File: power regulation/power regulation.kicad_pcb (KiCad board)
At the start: 4 copper layers, 175 x 100 mm, 90 parts, among them J1 Conn_01x02_Pin, J2 Conn_01x02_Pin, J3 Conn_01x02_Pin, M1 TO-236AB_SOT23_NEX, M2 TO-236AB_SOT23_NEX, U1 LT8640SEV_PBF, U2 LT8640SEV_PBF, U3 LT8619EDD-TRPBF

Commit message: start work on clearance fixes.
modified 8V regulator footprint, added not MAX rtd module not connected.
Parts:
- added REF**: QFN65P500X500X80-21N_MAXRTD_Pinless, Library:QFN65P500X500X80-21N_MAXRTD_Pinless, F.Cu at (239.2, 88.1)

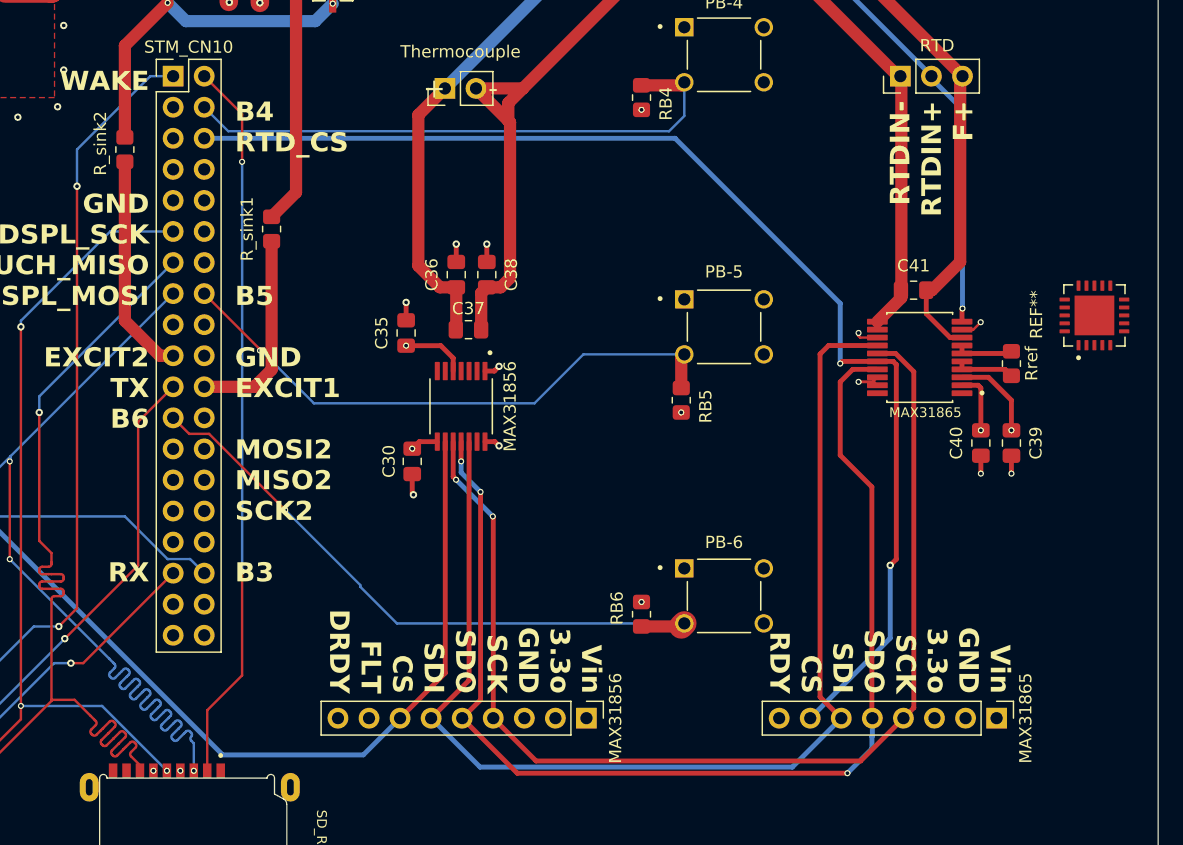
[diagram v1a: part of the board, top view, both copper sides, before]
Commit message: Fully integrate new Max RTD module.
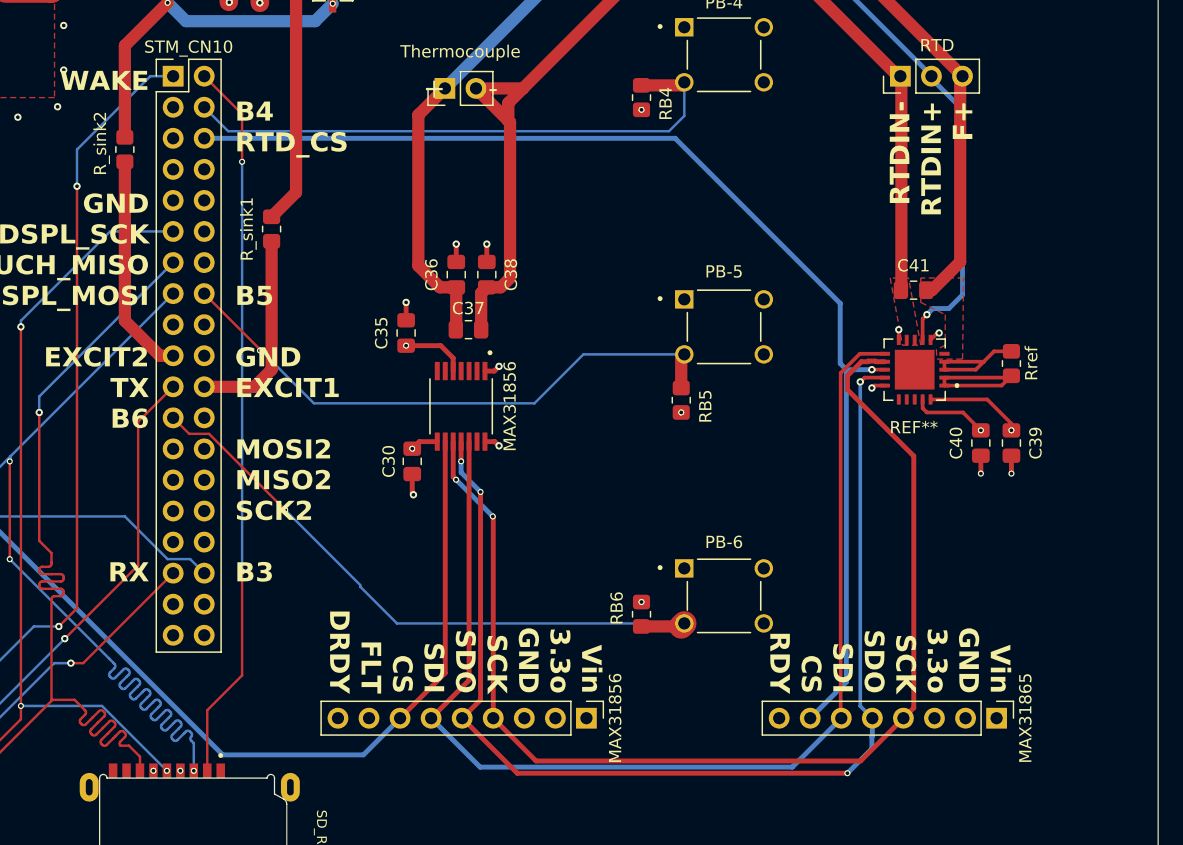
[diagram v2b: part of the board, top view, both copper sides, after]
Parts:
- removed the MAX31865 at (224.9, 91.5)
- moved REF** 15.4 mm to (224.5, 92.5), turned to 180 degrees
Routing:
- net BIAS: track 4.91 -> 12.0 mm
- net RTD+: track 44.6 -> 38.9 mm
- net ISENSOR: track 4.76 -> 9.96 mm
- net GND: track 120.7 -> 116.6 mm
- net RTD-: track 39.9 -> 35.9 mm
- net RTDSens: track 38.1 -> 41.7 mm
- net RTD_CS: track 99.1 -> 96.1 mm, vias 2 -> 1
- net MAX_SDI: track 96.2 -> 93.3 mm
- net MAX_SDO: track 94.7 -> 92.7 mm, vias 3 -> 4
- net MAX_SCK: track 92.7 -> 94.6 mm
- net /3.3V: track 92.9 -> 94.7 mm
- added copper zone on F.Cu, net RTD+
- added copper zone on F.Cu, net RTD-

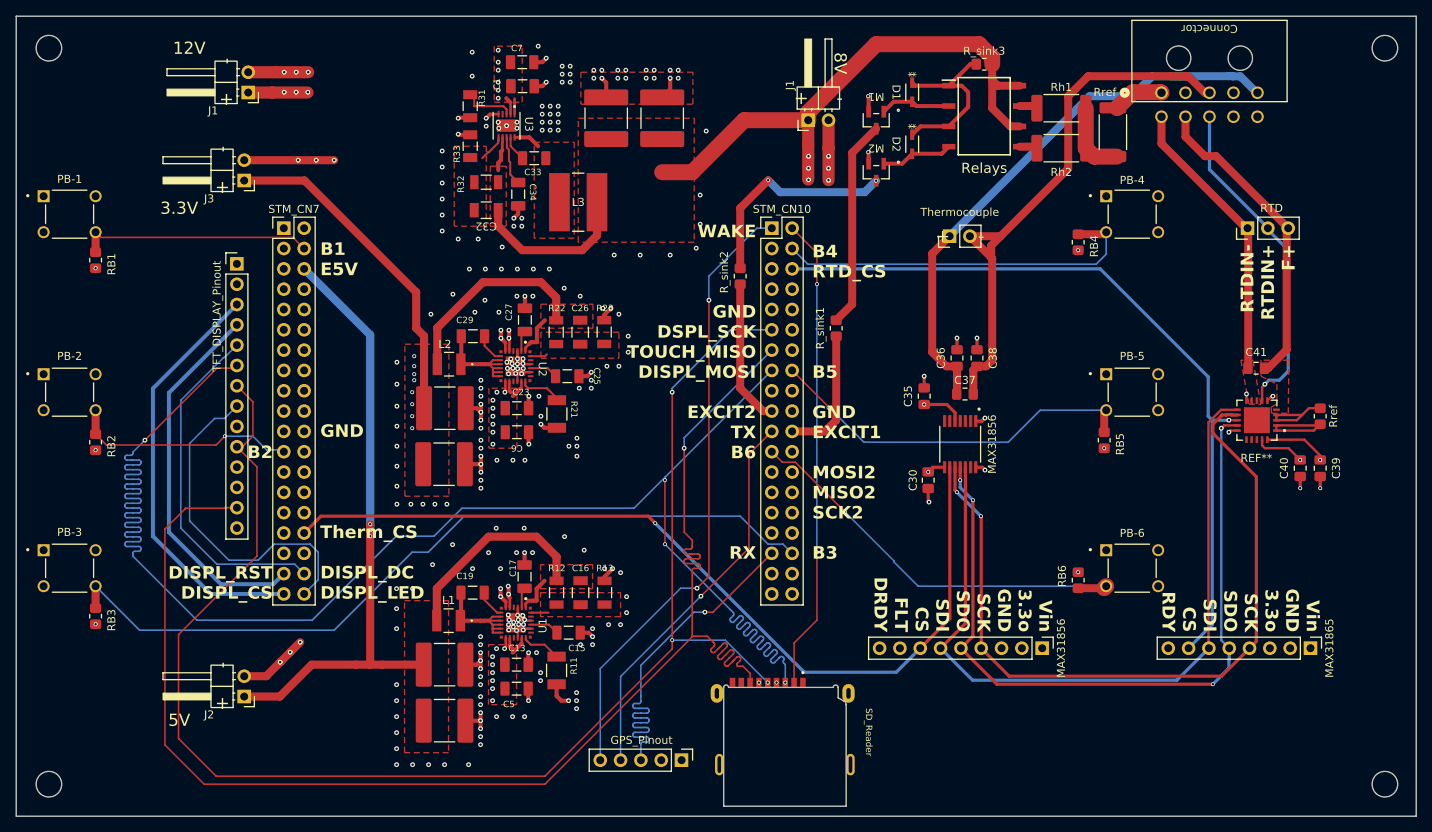
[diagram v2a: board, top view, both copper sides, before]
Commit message: Add holes for screen.
Moved traces and a couple comonents to accomodate.
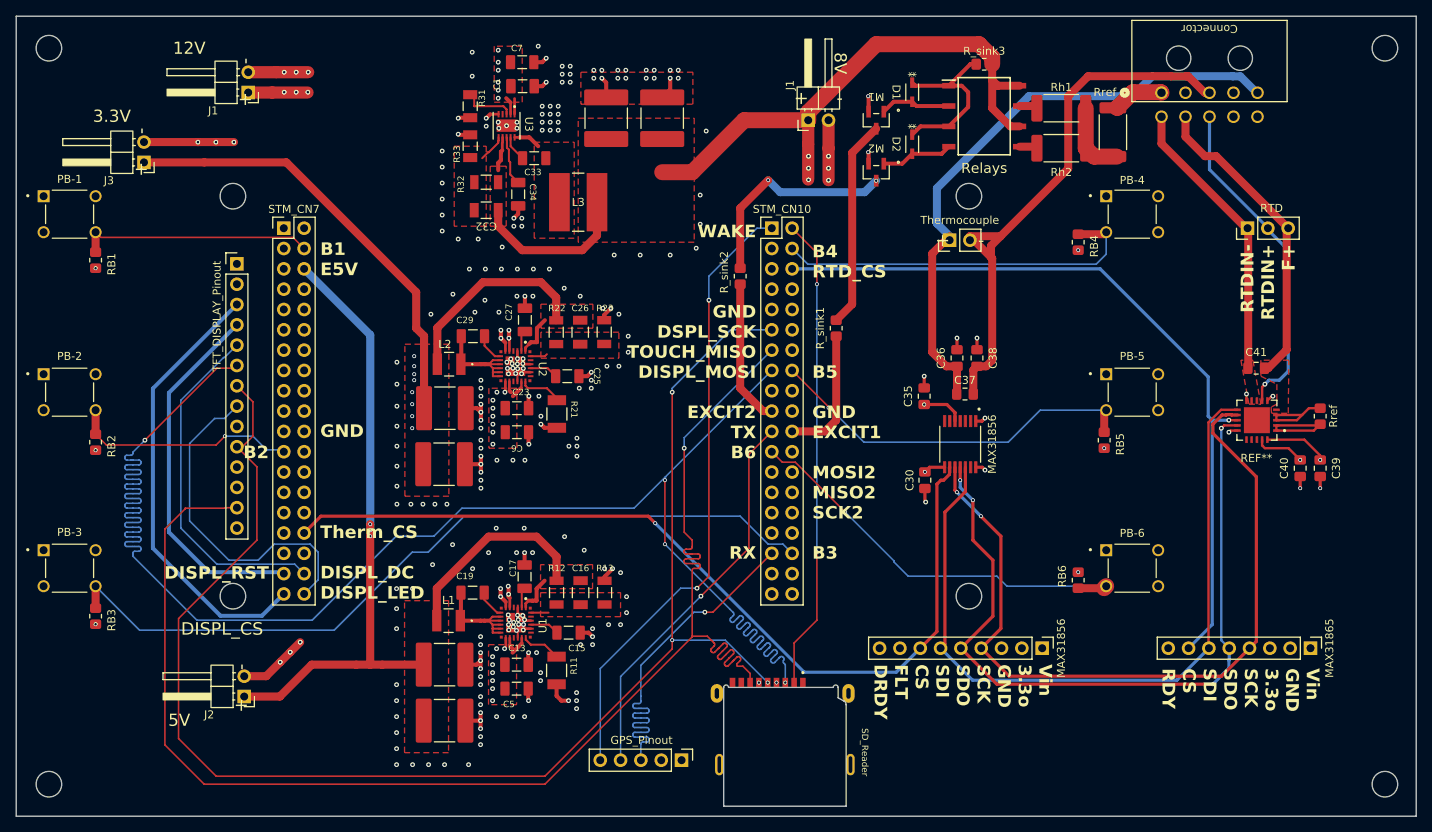
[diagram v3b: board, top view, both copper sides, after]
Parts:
- added hole: MountingHole_3.2mm_M3, MountingHole:MountingHole_3.2mm_M3, F.Cu at (96.5, 64.5)
- added hole: MountingHole_3.2mm_M3, MountingHole:MountingHole_3.2mm_M3, F.Cu at (188.5, 114.5)
- added hole: MountingHole_3.2mm_M3, MountingHole:MountingHole_3.2mm_M3, F.Cu at (188.5, 64.5)
- added hole: MountingHole_3.2mm_M3, MountingHole:MountingHole_3.2mm_M3, F.Cu at (96.5, 114.5)
- moved J3 12.7 mm to (85.4, 60.3)
- moved Thermocouple 0.50 mm to (186.1, 70.0)
- moved C30 0.41 mm to (183.0, 100.0)
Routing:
- net /3.3V: track 94.7 -> 108.6 mm
- net Thermocouple+: track 70.4 -> 76.1 mm
- net DISPL_CS: track 52.7 -> 55.8 mm
- net MAX_SDO: track 92.7 -> 94.8 mm
- net MAX_SCK: track 94.6 -> 96.6 mm
- net DISPL_RST: track 47.0 -> 45.9 mm
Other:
- board text added: "B2 DISPL_RST"
- board text added: "DISPL_CS"
- board text removed: "B2 DISPL_RST DISPL_CS"

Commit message: Connect Max modules to STM header.
Also added so extra silkscreening.
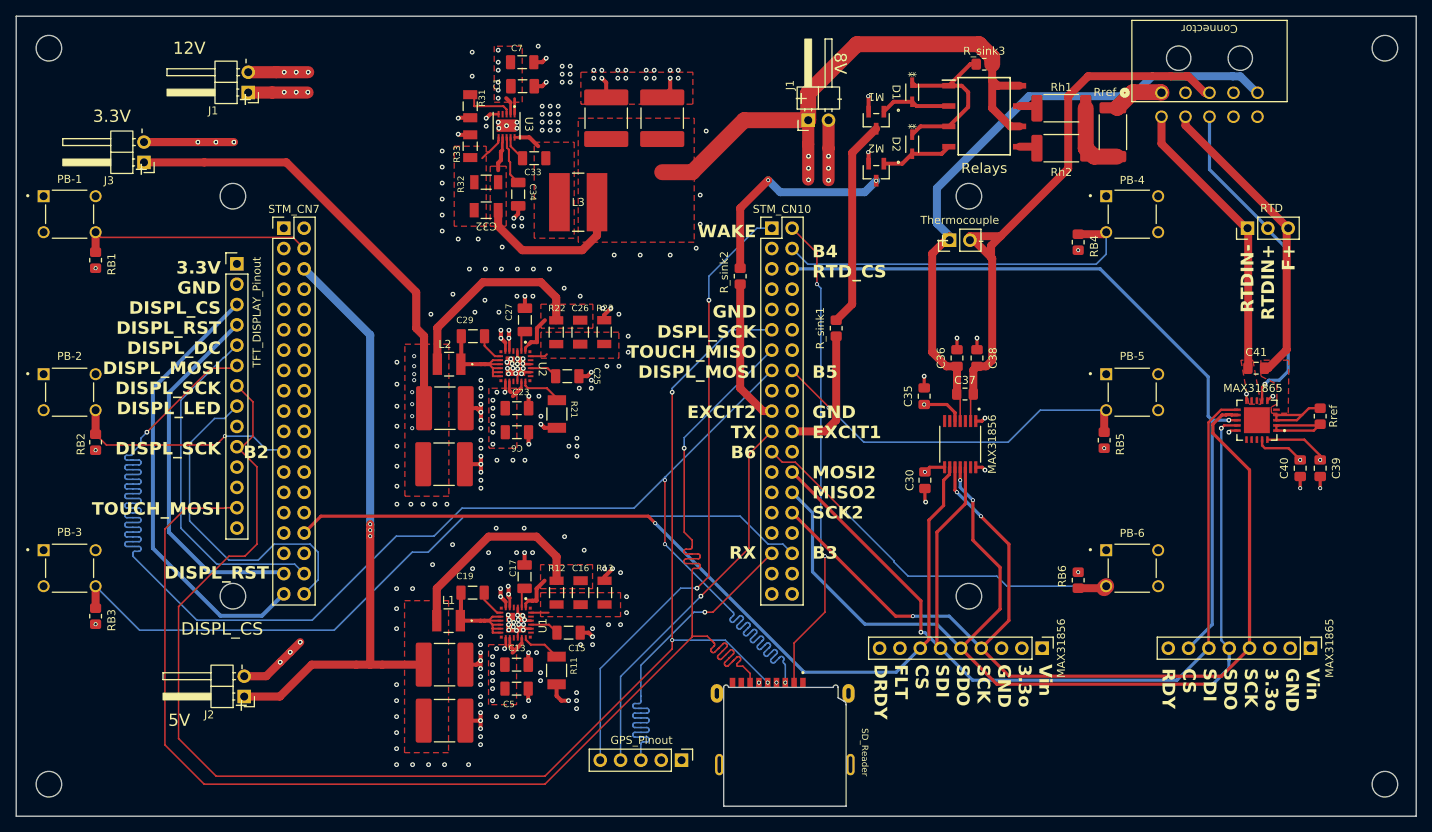
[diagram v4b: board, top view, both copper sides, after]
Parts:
- renumbered REF** to MAX31865
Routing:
- net MAX_SDO: track 94.8 -> 129.0 mm
- net MAX_SCK: track 96.6 -> 127.4 mm, vias 2 -> 3
- net MAX_SDI: track 93.3 -> 123.6 mm, vias 0 -> 1
- net Thermocouple+: track 76.1 -> 79.7 mm
- net Thermocouple-: track 70.3 -> 73.8 mm
- net /8V: track 97.3 -> 98.7 mm
- net DISPL_SCK: track 183.7 -> 184.9 mm
- net SD_CS: track 59.3 -> 60.1 mm
- net RTD+: track 38.9 -> 38.1 mm
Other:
- board text added: "3.3V GND DISPL_CS DISPL_RST DISPL_DC DISPL_MOSI DISPL_SCK DISPL_LED DISPL_SCK TOUCH_MOSI"

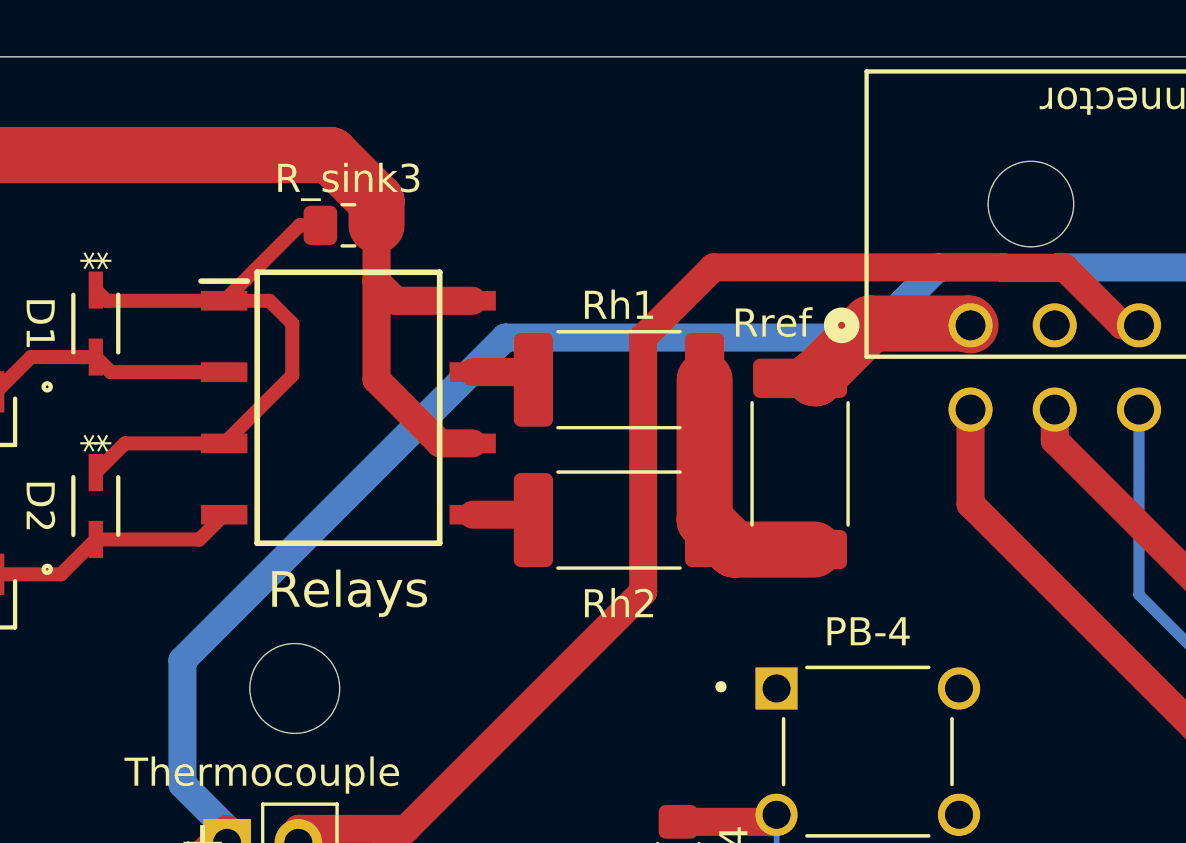
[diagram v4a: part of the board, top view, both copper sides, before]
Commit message: Add header for measuring exciter current.
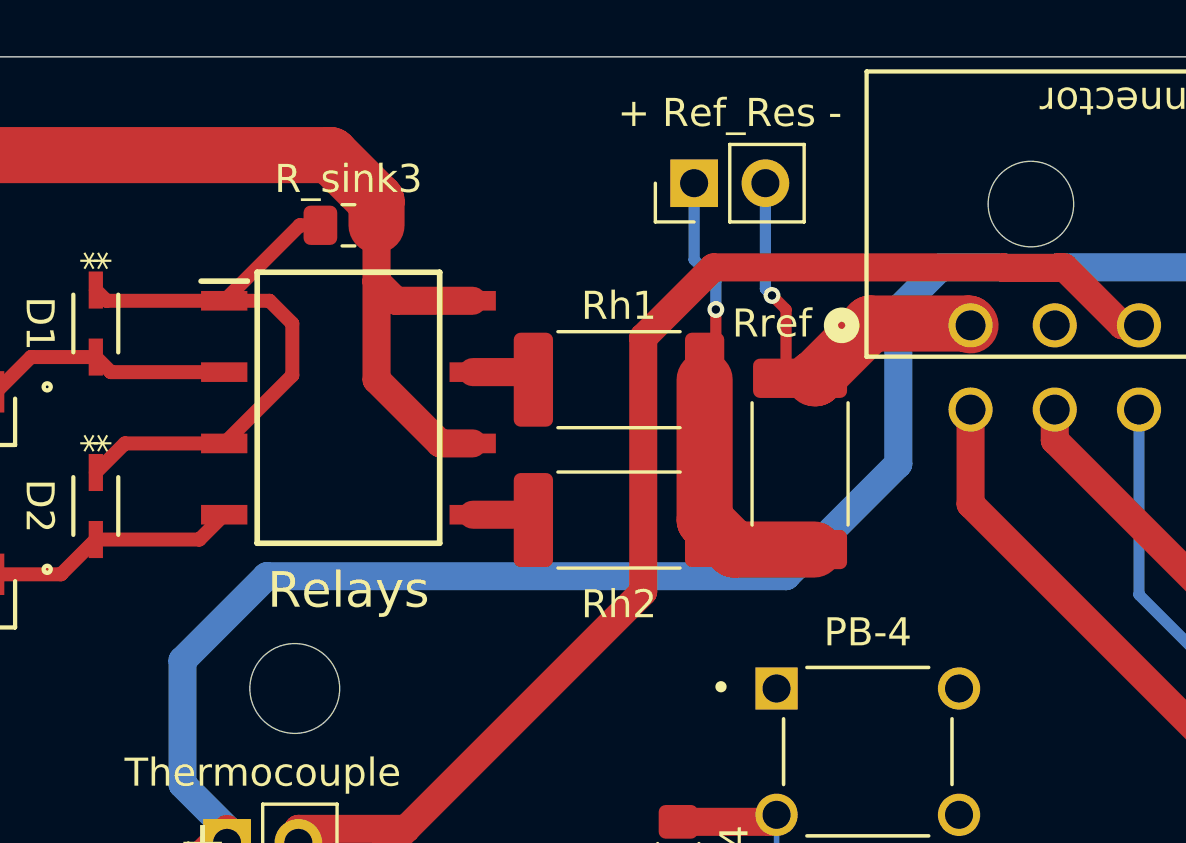
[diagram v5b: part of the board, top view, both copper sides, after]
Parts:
- added + Ref_Res -: PinHeader_1x02_P2.54mm_Vertical, Connector_PinHeader_2.54mm:PinHeader_1x02_P2.54mm_Vertical, F.Cu at (202.7, 46.5)
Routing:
- net HeaterPre: track 9.33 -> 16.8 mm, vias 0 -> 1
- net Heater+: track 6.41 -> 13.9 mm, vias 0 -> 1
- net Thermocouple+: track 79.7 -> 82.9 mm
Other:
- board text added: "- Ref_Res +"

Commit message: Add label silkscreen
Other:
- board text added: "C-Therm TLS Handheld System PCB"
- board text added: "C-Therm TLS Handheld System PCB :)"
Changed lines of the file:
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@@
 	)
 	(paper "A4")
+	(title_block
+		(title "TLS Handheld System PCB")
+		(date "2026-01-28")
+		(rev "1")
+		(company "C-Therm Technologies")
+		(comment 1 "Designers - Connor Yerxa, Faaiz Ali, Marc-Andre Bourgoin")
+	)
 	(layers
 		(0 "F.Cu" signal)
@@
 		)
 	)
+	(gr_text "C-Therm TLS Handheld System PCB"
+		(at 181.5 140 0)
+		(layer "F.SilkS")
+		(effects
+			(font
+				(size 2 2)
+				(thickness 0.3)
+			)
+			(justify left bottom)
+		)
+	)
 	(gr_text "B4\nRTD_CS\n\n\n\n\nB5\n\nGND\nEXCIT1\n\nMOSI2\nMISO2\nSCK2\n\nB3"
 		(at 169 110 0)
@@
 		)
 	)
+	(gr_text "C-Therm TLS Handheld System PCB :)"
+		(at 177.5 140 0)
+		(layer "B.SilkS")
+		(effects
+			(font
+				(size 2 2)
+				(thickness 0.3)
+			)
+			(justify right bottom mirror)
+		)
+	)

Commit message: stuff
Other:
- board text added: "ftl"
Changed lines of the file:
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@@
+		)
+	)
+	(gr_text "ftl"
+		(at 187 95.5 0)
+		(layer "F.SilkS")
+		(effects
+			(font
+				(size 0.8 0.8)
+				(thickness 0.1)
+			)
+			(justify left bottom)
 		)
 	)
